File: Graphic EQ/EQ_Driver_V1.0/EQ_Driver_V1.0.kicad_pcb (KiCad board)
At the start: 2 copper layers, 127 x 57.2 mm, 35 parts, among them Q1 MPSA63, Q2 MPSA70, Q3 MPSA70, Q4 MPSA20

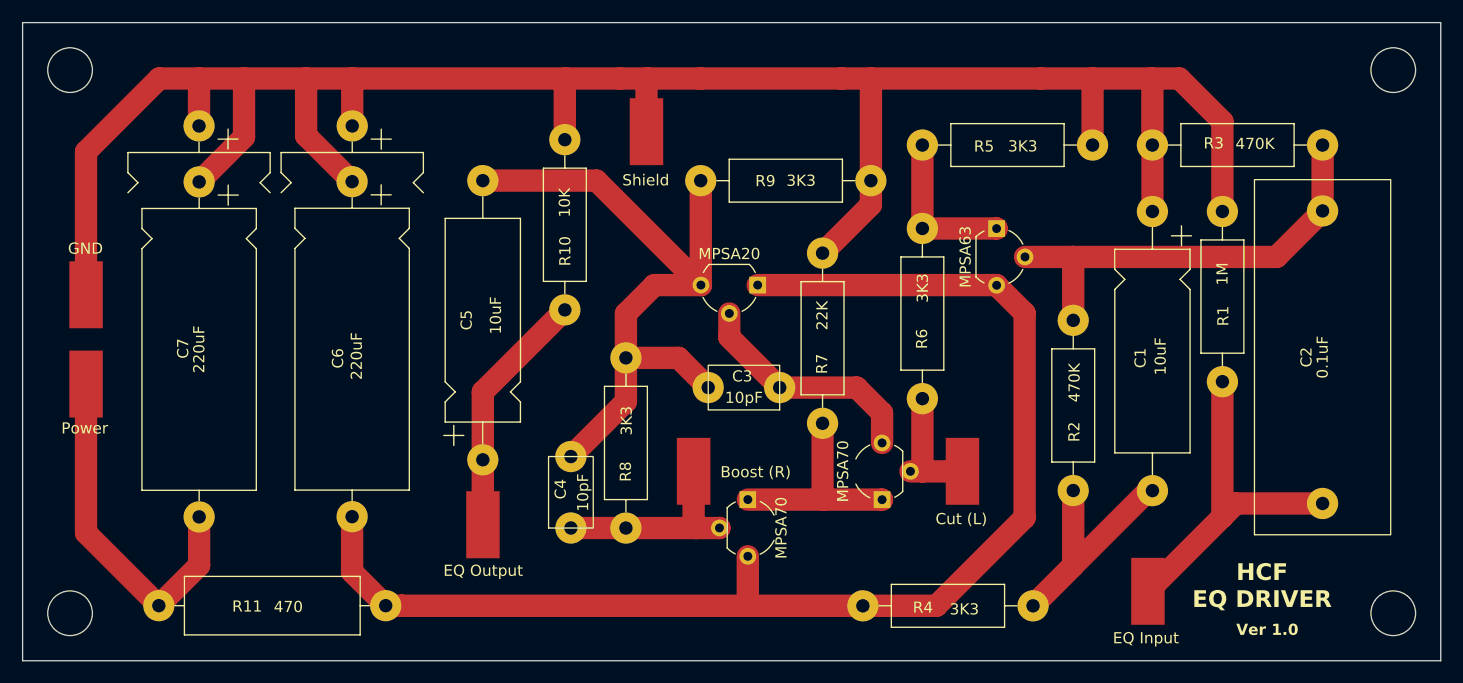
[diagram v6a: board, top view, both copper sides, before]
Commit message: Adjusted Resistor Sizes
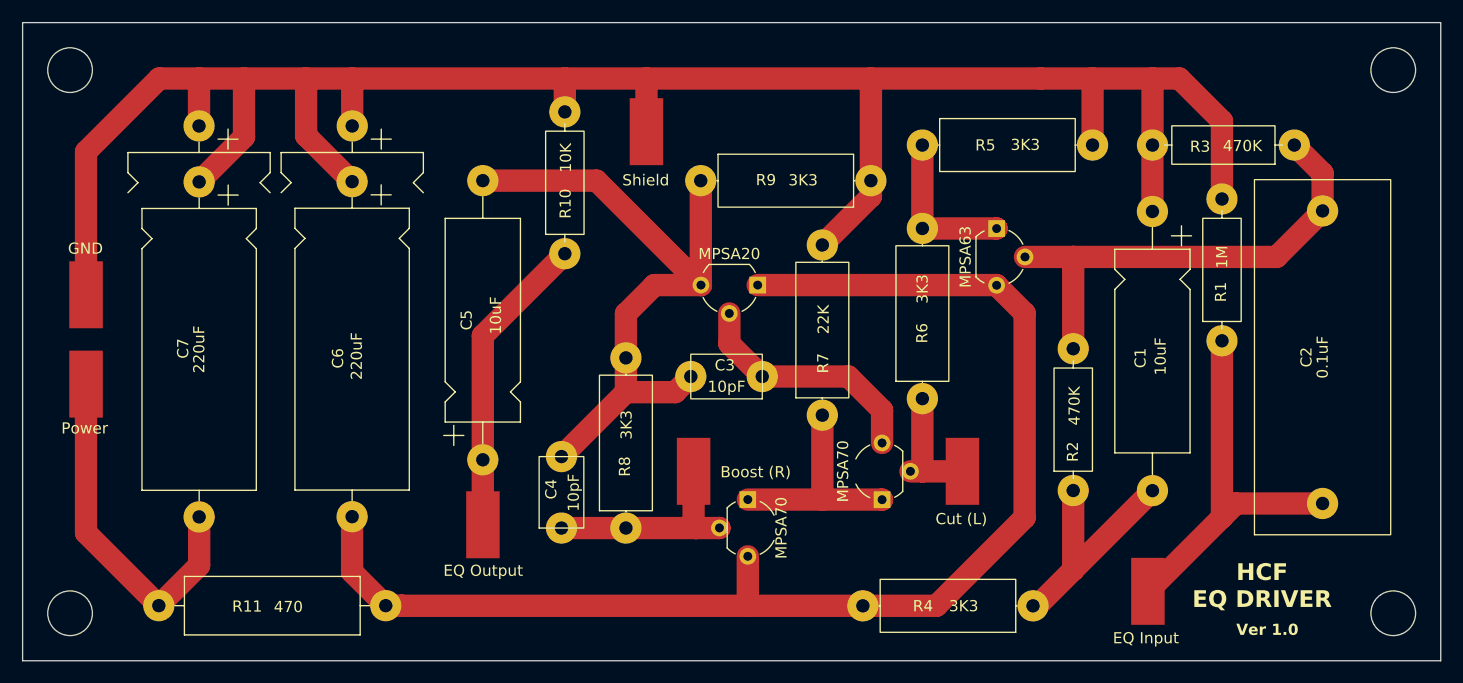
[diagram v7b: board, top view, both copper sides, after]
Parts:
- R1, R10, R2, R3: footprint Resistor_THT:R_Axial_DIN0411_L9.9mm_D3.6mm_P15.24mm_Horizontal -> Resistor_THT:R_Axial_DIN0309_L9.0mm_D3.2mm_P12.70mm_Horizontal
- R4, R5, R6, R7, R8, R9: footprint Resistor_THT:R_Axial_DIN0411_L9.9mm_D3.6mm_P15.24mm_Horizontal -> Resistor_THT:R_Axial_DIN0414_L11.9mm_D4.5mm_P15.24mm_Horizontal
- moved R10 5.03 mm to (126.3, 86.1)
- moved R1 3.66 mm to (185.2, 93.9)
- moved R3 2.53 mm to (191.6, 76.3)
- moved C3 1.85 mm to (144.0, 97.1)
- moved C4 0.84 mm to (126.0, 110.6)
- moved R7 0.73 mm to (149.4, 100.5)
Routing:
- net Net-(C5-Pad1): track 22.3 -> 27.3 mm
- net Net-(C1-Pad2): track 26.8 -> 22.1 mm
- net GND: track 203.3 -> 198.8 mm
- net Net-(C2-Pad1): track 31.0 -> 34.7 mm
- net Net-(Q1-B): track 39.9 -> 43.5 mm
- net Net-(Q4-C): track 63.9 -> 62.1 mm
- net Net-(Q3-B): track 18.5 -> 19.3 mm
- net Net-(Q2-E): track 18.9 -> 19.6 mm

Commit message: Preamp Progress, and Custom Footprint Library
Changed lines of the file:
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@@
-	)
-	(segment
-		(start 153.72 70.38)
-		(end 168.94 70.38)
-		(width 2)
-		(layer "F.Cu")
-		(net 2)
 	)
 	(segment
@@
 	)
 	(segment
-		(start 168.94 70.38)
+		(start 153.72 70.38)
 		(end 173.55 70.38)
 		(width 2)
@@
 		(width 2)
 		(layer "F.Cu")
-		(net 6)
-	)
-	(segment
-		(start 118.9671 79.53)
-		(end 118.9643 79.5272)
-		(width 2)
-		(layer "F.Cu")
